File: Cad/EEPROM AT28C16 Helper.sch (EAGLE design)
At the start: 6 parts

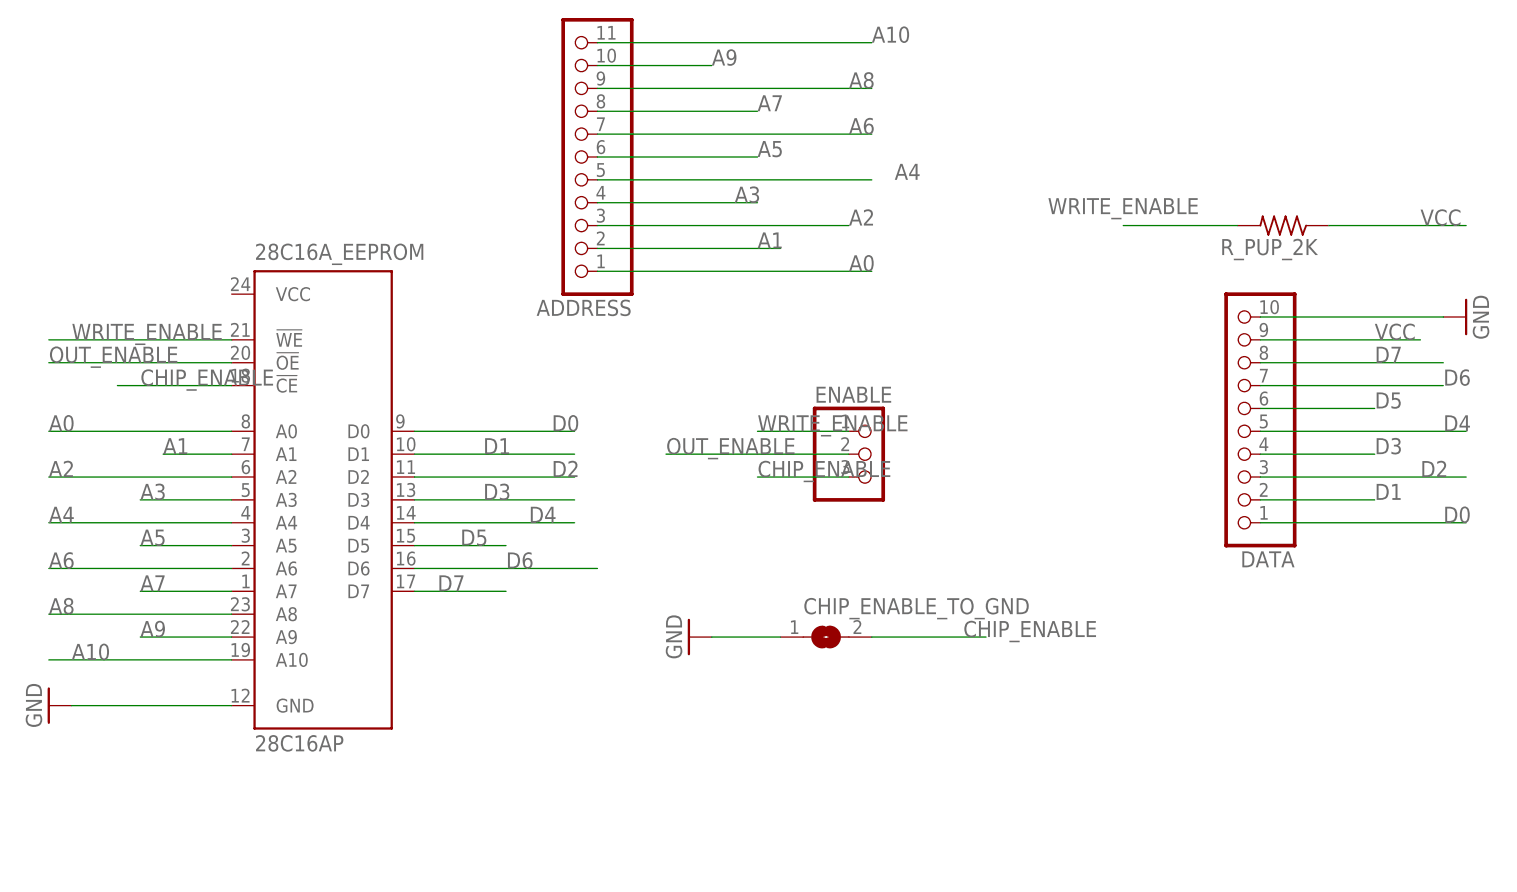
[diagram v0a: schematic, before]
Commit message: Update code now that we have the eeprom programmer board
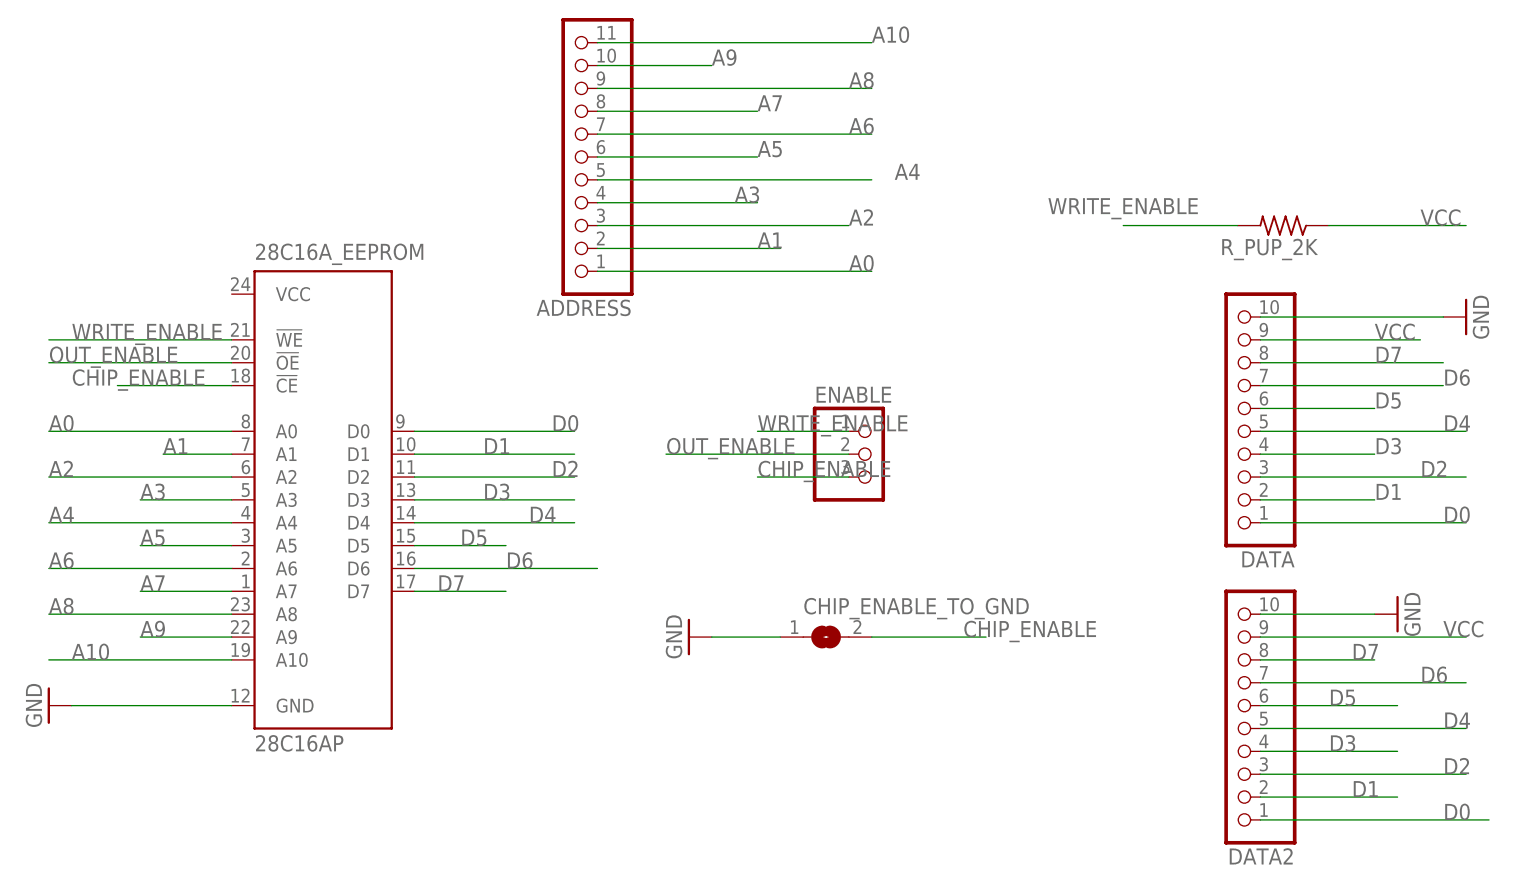
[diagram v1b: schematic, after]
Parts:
- added DATA2: PINHD-1X10, adafruit:PINHD-1X10
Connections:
- net D0: now also DATA2.1
- net D1: now also DATA2.2
- net D2: now also DATA2.3
- net D3: now also DATA2.4
- net D4: now also DATA2.5
- net D5: now also DATA2.6
- net D6: now also DATA2.7
- net D7: now also DATA2.8
- net GND: now also DATA2.10
- net VCC: now also DATA2.9
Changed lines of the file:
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@@
 <part name="CHIP_ENABLE_TO_GND" library="microbuilder" deviceset="SOLDERJUMPER" device="REFLOW"/>
 <part name="GND1" library="supply1" deviceset="GND" device=""/>
+<part name="DATA2" library="adafruit" deviceset="PINHD-1X10" device=""/>
+<part name="GND2" library="supply1" deviceset="GND" device=""/>
 </parts>
 <sheets>
@@
 <instance part="CHIP_ENABLE_TO_GND" gate="1" x="2.54" y="33.02"/>
 <instance part="GND1" gate="1" x="-12.7" y="33.02" rot="R270"/>
+<instance part="DATA2" gate="G$1" x="48.26" y="22.86" smashed="yes" rot="R180">
+<attribute name="NAME" x="54.61" y="9.525" size="1.778" layer="95" rot="R180"/>
+</instance>
+<instance part="GND2" gate="1" x="66.04" y="35.56" rot="R90"/>
 </instances>
 <busses>
@@
 <wire x1="-2.54" y1="33.02" x2="-10.16" y2="33.02" width="0.1524" layer="91"/>
 </segment>
+<segment>
+<pinref part="DATA2" gate="G$1" pin="10"/>
+<pinref part="GND2" gate="1" pin="GND"/>
+<wire x1="50.8" y1="35.56" x2="63.5" y2="35.56" width="0.1524" layer="91"/>
+</segment>
 </net>
 <net name="VCC" class="0">
@@
 <label x="63.5" y="66.04" size="1.778" layer="95"/>
 </segment>
+<segment>
+<pinref part="DATA2" gate="G$1" pin="9"/>
+<wire x1="50.8" y1="33.02" x2="73.66" y2="33.02" width="0.1524" layer="91"/>
+<label x="71.12" y="33.02" size="1.778" layer="95"/>
+</segment>
 </net>
 <net name="D0" class="0">
@@
 <label x="71.12" y="45.72" size="1.778" layer="95"/>
 </segment>
+<segment>
+<pinref part="DATA2" gate="G$1" pin="1"/>
+<wire x1="50.8" y1="12.7" x2="76.2" y2="12.7" width="0.1524" layer="91"/>
+<label x="71.12" y="12.7" size="1.778" layer="95"/>
+</segment>
 </net>
 <net name="D1" class="0">
@@
 <label x="63.5" y="48.26" size="1.778" layer="95"/>
 </segment>
+<segment>
+<pinref part="DATA2" gate="G$1" pin="2"/>
+<wire x1="50.8" y1="15.24" x2="66.04" y2="15.24" width="0.1524" layer="91"/>
+<label x="60.96" y="15.24" size="1.778" layer="95"/>
+</segment>
 </net>
 <net name="D2" class="0">
@@
 <label x="68.58" y="50.8" size="1.778" layer="95"/>
 </segment>
+<segment>
+<pinref part="DATA2" gate="G$1" pin="3"/>
+<wire x1="50.8" y1="17.78" x2="73.66" y2="17.78" width="0.1524" layer="91"/>
+<label x="71.12" y="17.78" size="1.778" layer="95"/>
+</segment>
 </net>
 <net name="D3" class="0">
@@
 <label x="63.5" y="53.34" size="1.778" layer="95"/>
 </segment>
+<segment>
+<pinref part="DATA2" gate="G$1" pin="4"/>
+<wire x1="50.8" y1="20.32" x2="66.04" y2="20.32" width="0.1524" layer="91"/>
+<label x="58.42" y="20.32" size="1.778" layer="95"/>
+</segment>
 </net>
 <net name="D4" class="0">
@@
 <label x="71.12" y="55.88" size="1.778" layer="95"/>
 </segment>
+<segment>
+<pinref part="DATA2" gate="G$1" pin="5"/>
+<wire x1="50.8" y1="22.86" x2="73.66" y2="22.86" width="0.1524" layer="91"/>
+<label x="71.12" y="22.86" size="1.778" layer="95"/>
+</segment>
 </net>
 <net name="A10" class="0">
@@
 <label x="63.5" y="58.42" size="1.778" layer="95"/>
 </segment>
+<segment>
+<pinref part="DATA2" gate="G$1" pin="6"/>
+<wire x1="50.8" y1="25.4" x2="66.04" y2="25.4" width="0.1524" layer="91"/>
+<label x="58.42" y="25.4" size="1.778" layer="95"/>
+</segment>
 </net>
 <net name="D6" class="0">
@@
 <label x="71.12" y="60.96" size="1.778" layer="95"/>
 </segment>
+<segment>
+<pinref part="DATA2" gate="G$1" pin="7"/>
+<wire x1="50.8" y1="27.94" x2="73.66" y2="27.94" width="0.1524" layer="91"/>
+<label x="68.58" y="27.94" size="1.778" layer="95"/>
+</segment>
 </net>
 <net name="D7" class="0">
@@
 <label x="63.5" y="63.5" size="1.778" layer="95"/>
 </segment>
+<segment>
+<pinref part="DATA2" gate="G$1" pin="8"/>
+<wire x1="50.8" y1="30.48" x2="63.5" y2="30.48" width="0.1524" layer="91"/>
+<label x="60.96" y="30.48" size="1.778" layer="95"/>
+</segment>
 </net>
 <net name="CHIP_ENABLE" class="0">
@@
 <pinref part="28C16A_EEPROM" gate="G$1" pin="!CE"/>
 <wire x1="-63.5" y1="60.96" x2="-76.2" y2="60.96" width="0.1524" layer="91"/>
-<label x="-73.66" y="60.96" size="1.778" layer="95"/>
-</segment>
-<segment>
+<label x="-81.28" y="60.96" size="1.778" layer="95"/>
+</segment>
+<segment>
